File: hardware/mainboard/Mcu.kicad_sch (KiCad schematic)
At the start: 14 parts, among them J2 XIAO ESP32S3 Sense, U1 MAX40200AUK, U10 STM32H573RITx

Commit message: Layout again
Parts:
- added TP2, TP3: TestPoint_Small, TestPoint:TestPoint_Pad_D1.0mm, symbol Connector:TestPoint_Small
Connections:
- net +3.3VMCU: now also TP3.1
- net 3.3V_PROT: now also TP2.1

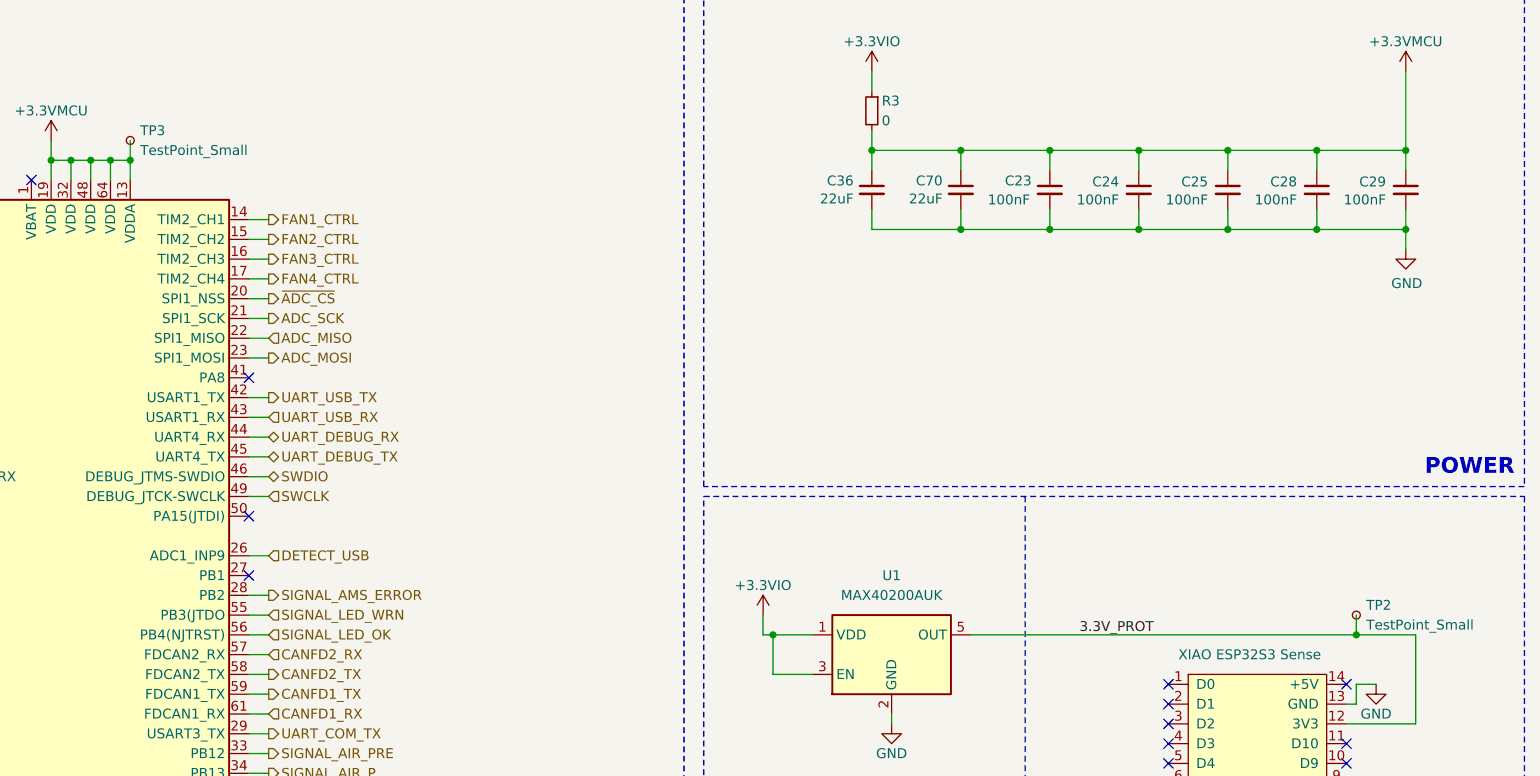
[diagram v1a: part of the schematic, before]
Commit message: Plytka chyba fajnie zrobiona oprocz teardropow bo kicad 10 jest dziwny
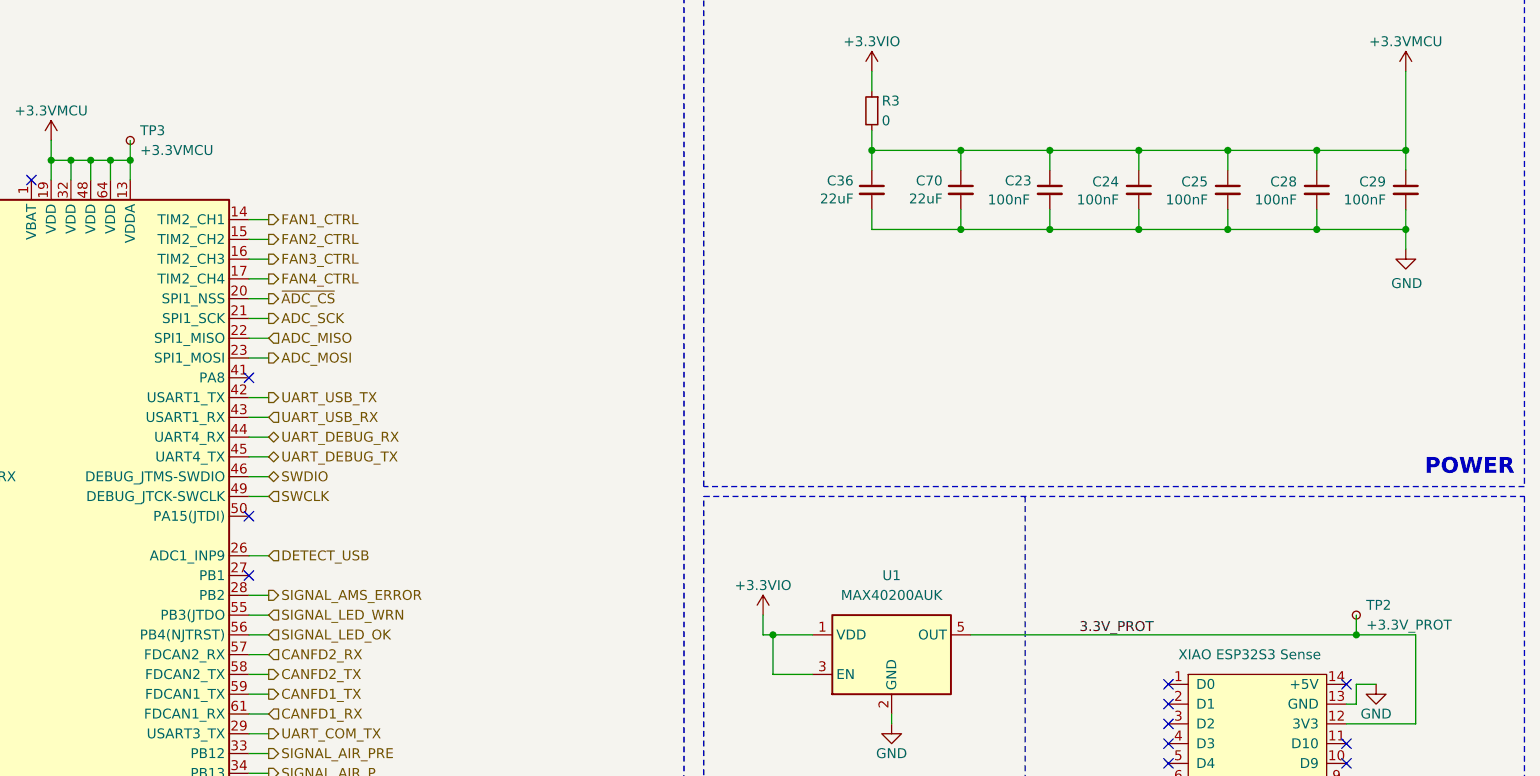
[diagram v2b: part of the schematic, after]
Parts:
- TP2: value TestPoint_Small -> +3.3V_PROT
- TP3: value TestPoint_Small -> +3.3VMCU

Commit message: sync
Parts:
- removed TP2: +3.3V_PROT, TestPoint:TestPoint_Pad_D1.0mm, symbol Connector:TestPoint_Small
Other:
- note removed: "backcurrent protection"
- note removed: "μC"
